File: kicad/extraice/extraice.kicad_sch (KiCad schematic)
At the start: 71 parts, among them J1 Conn_01x02, J10 Conn_01x02, J3 EncSide, J4 MainSide, J5 Conn_01x05, J6 EncSide, J7 MainSide, J8 Conn_01x02, J9 Conn_01x02, Q1 L-31ROPT1C, Q2 L-31ROPT1C, Q3 L-31ROPT1C, Q4 L-31ROPT1C, SW1 PCM12SMTR, SW2 B3U-1000P, U1 DG2034EDN, U10 DRV8837C, U11 DRV8837C, U12 AS5047D, U2 BCR421, U3 MUN12AD01-SG, U4 MB85RC64TA, U5 LSM6DSR, U6 XC6221B302GR, U7 ESP32-S3-FN8, U8 AS5047D, U9 DRV8837C, X1 830108208709

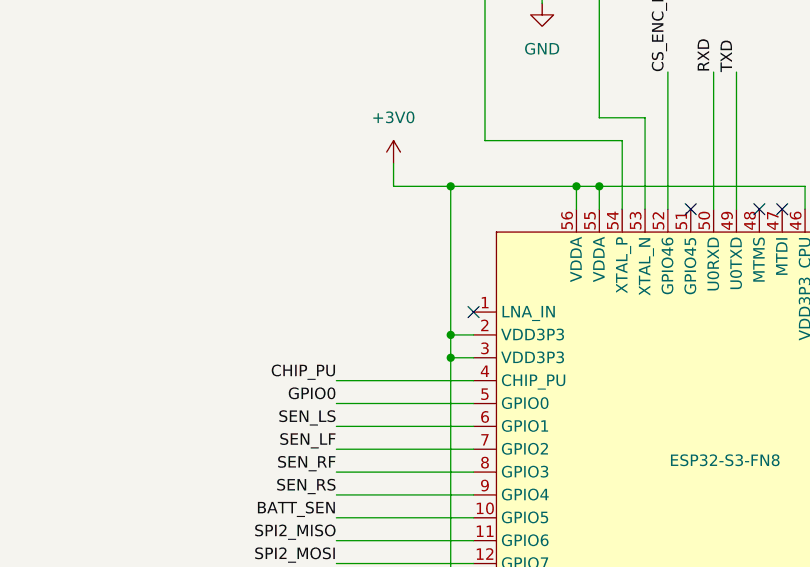
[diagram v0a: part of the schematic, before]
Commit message: Add a pull-up register to the CHIP-PU pin.
Signed-off-by: Kazuki Iida <elkel53930@gmail.com>
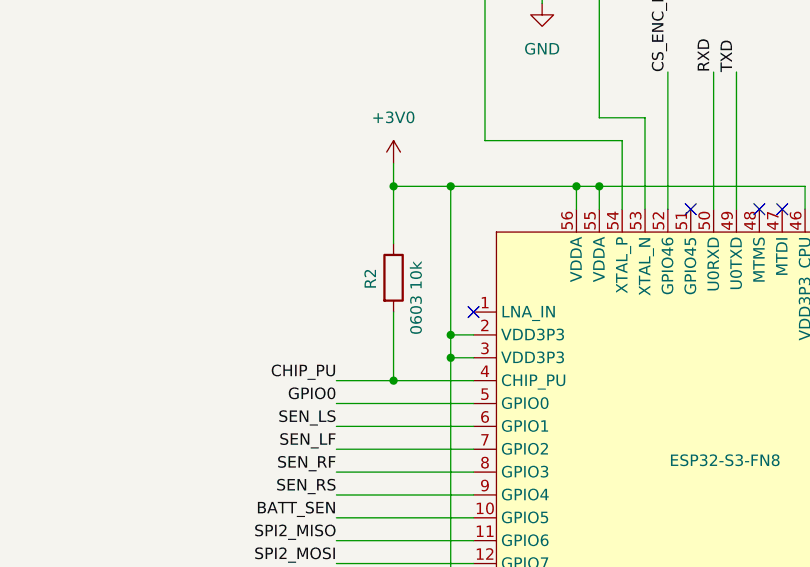
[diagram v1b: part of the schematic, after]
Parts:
- added R2: 0603 10k, Resistor_SMD:R_0201_0603Metric, symbol Device:R
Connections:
- net +3V0: now also R2.1
- net CHIP_PU: now also R2.2
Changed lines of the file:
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@@
   (junction (at 158.75 168.91) (diameter 0) (color 0 0 0 0)
   )
+  (junction (at 209.55 125.73) (diameter 0) (color 0 0 0 0)
+  )
   (junction (at 281.94 234.95) (diameter 0) (color 0 0 0 0)
   )
@@
   (junction (at 91.44 237.49) (diameter 0) (color 0 0 0 0)
   )
+  (junction (at 209.55 104.14) (diameter 0) (color 0 0 0 0)
+  )
   (junction (at 189.23 180.34) (diameter 0) (color 0 0 0 0)
   )
@@
     (stroke (width 0) (type default))
   )
+  (wire (pts (xy 209.55 118.11) (xy 209.55 125.73))
+    (stroke (width 0) (type default))
+  )
   (wire (pts (xy 68.58 232.41) (xy 71.12 232.41))
     (stroke (width 0) (type default))
@@
     (stroke (width 0) (type default))
   )
-  (wire (pts (xy 203.2 125.73) (xy 218.44 125.73))
+  (wire (pts (xy 203.2 125.73) (xy 209.55 125.73))
     (stroke (width 0) (type default))
   )
@@
     (stroke (width 0) (type default))
   )
+  (wire (pts (xy 209.55 125.73) (xy 218.44 125.73))
+    (stroke (width 0) (type default))
+  )
   (wire (pts (xy 377.19 107.95) (xy 375.92 107.95))
     (stroke (width 0) (type default))
@@
     (stroke (width 0) (type default))
   )
+  (wire (pts (xy 209.55 104.14) (xy 209.55 110.49))
+    (stroke (width 0) (type default))
+  )
   (wire (pts (xy 375.92 158.75) (xy 375.92 165.1))
     (stroke (width 0) (type default))
@@
         )
       )
+    )
+  )
+  (symbol (lib_id "Device:R") (at 209.55 114.3 0) (unit 1)
+    (in_bom yes) (on_board yes) (dnp no)
+    (property "Reference" "R2" (at 207.01 115.57 90)
+      (effects (font (size 1.27 1.27)) (justify left))
+    )
+    (property "Value" "0603 10k" (at 212.09 120.65 90)
+      (effects (font (size 1.27 1.27)) (justify left))
+    )
+    (property "Footprint" "Resistor_SMD:R_0201_0603Metric" (at 207.772 114.3 90)
+      (effects (font (size 1.27 1.27)) hide)
+    )
+    (property "Datasheet" "~" (at 209.55 114.3 0)
+      (effects (font (size 1.27 1.27)) hide)
+    )
+    (pin "1")
+    (pin "2")
+    (instances
+      (project "extraice"
+        (path "/758e42d9-0381-4d70-87c4-16282301b5b4"
+          (reference "R2") (unit 1)
+        )
+      )

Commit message: Artwork for 4A completed
Need to check details.

Signed-off-by: Kazuki Iida <elkel53930@gmail.com>
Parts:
- removed C14, C15, C16, C5: 0603 50V 0.1uF, Capacitor_SMD:C_0201_0603Metric, symbol Device:C_Small
- removed J1: Conn_01x02, Micromouse:B2B-ZH, symbol Connector_Generic:Conn_01x02
- removed R14, R15, R16: 0603 10k, Resistor_SMD:R_0201_0603Metric, symbol Device:R
- removed SW2: B3U-1000P, Button_Switch_SMD:SW_SPST_B3U-1000P, symbol Switch:SW_Push
- removed U4: MB85RC64TA, Library:LCC-8P-M04, symbol micromouse:MB85RC64TA
- removed X1: 830108208709, Oscillator:Oscillator_SMD_ECS_2520MV-xxx-xx-4Pin_2.5x2.0mm, symbol Device:Crystal_GND24
- added C6: 1608 10V 4.7uF, Capacitor_SMD:C_0603_1608Metric, symbol Device:C_Small
- added D8: 1608 R LED, LED_SMD:LED_0603_1608Metric, symbol Device:LED
- added J1, J2: Conn_01x03, Connector_PinHeader_2.00mm:PinHeader_1x03_P2.00mm_Vertical, symbol Connector_Generic:Conn_01x03
- added R3: 0603 10k, Resistor_SMD:R_0201_0603Metric, symbol Device:R
- C11, C13: value 1005 N/M -> 1608 10V 4.7uF; footprint Capacitor_SMD:C_0402_1005Metric -> Capacitor_SMD:C_0603_1608Metric
- C12: value 0603 50V 0.1uF -> 1608 10V 4.7uF; footprint Capacitor_SMD:C_0201_0603Metric -> Capacitor_SMD:C_0603_1608Metric
- C4: value 3225 25V 22uF -> 1608 10V 4.7uF; footprint Capacitor_SMD:C_1210_3225Metric -> Capacitor_SMD:C_0603_1608Metric
- R1, R10, R12, R7: value 0603 470 1% -> 1005 470 1%; footprint Resistor_SMD:R_0201_0603Metric -> Resistor_SMD:R_0402_1005Metric
- U7: value ESP32-S3-FN8 -> ESP32-S3-PICO-1-N8R2
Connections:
- net +3.3V: now also C11.2, C12.2, C13.2, C4.2, C6.2; no longer C4.1
- net +3V0: no longer C12.1
- net +BATT: now also SW1.2 (B), R3.2; no longer C21.1, SW1.3 (C), U10.1 (VM), U11.1 (VM), U9.1 (VM)
- net CS_ENC_L: now also U7.14 (GPIO9); no longer U7.15 (GPIO10)
- net CS_IMU: now also U7.27 (GPIO21); no longer U7.14 (GPIO9)
- net GND: now also C11.1, C12.1, C13.1, C4.1, C6.1, D8.1 (K), J2.1 (Pin_1); no longer C11.2, C12.2, C13.2, C4.2
- net LED_SEL0: now also U7.12 (GPIO7); no longer U7.21 (XTAL_32K_P)
- net LED_SEL1: now also U7.13 (GPIO8); no longer U7.22 (XTAL_32K_N)
- net SEN_LED_ENA: now also U7.11 (GPIO6); no longer U7.19 (GPIO14)
- net SEN_LF: now also U7.8 (GPIO3); no longer U7.7 (GPIO2)
- net SEN_LS: now also U7.9 (GPIO4); no longer U7.6 (GPIO1)
- net SEN_RF: now also U7.7 (GPIO2); no longer U7.8 (GPIO3)
- net SEN_RS: now also U7.6 (GPIO1); no longer U7.9 (GPIO4)
- net SPI1_MISO: now also U7.16 (GPIO11); no longer U7.17 (GPIO12)
- net SPI1_MOSI: now also U7.17 (GPIO12); no longer U7.18 (GPIO13)
- net SPI1_SCK: now also U7.15 (GPIO10); no longer U7.16 (GPIO11)
- net SPI2_MISO: now also U7.22 (XTAL_32K_N); no longer U7.11 (GPIO6)
- net SPI2_MOSI: now also U7.25 (GPIO19); no longer U7.12 (GPIO7)
- net SPI2_SCK: now also U7.26 (GPIO20); no longer U7.13 (GPIO8)
- net at U7.54 (XTAL_P): no longer C11.1
- net at U7.53 (XTAL_N): no longer C13.1
- net LED_FRONT_B renamed LED_B
- net LED_B: now also U7.21 (XTAL_32K_P); no longer U7.26 (GPIO20)
- net LED_LEFT_R renamed LED_R
- net LED_R: now also U7.18 (GPIO13); no longer U7.27 (GPIO21)
- net LED_RIGHT_G renamed LED_G
- net LED_G: now also U7.19 (GPIO14); no longer U7.25 (GPIO19)
- net SCL: no longer names the net of U7.23 (GPIO17)
- net SDA: no longer names the net of U7.24 (GPIO18)
- new net: D8.2 (A), R3.1
- new net: J1.1 (Pin_1), J2.3 (Pin_3)
- new net V_MOT: C21.1, J1.3 (Pin_3), SW1.3 (C), U10.1 (VM), U11.1 (VM), U9.1 (VM)
- no-connect marks 34 -> 40
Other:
- note removed: "Log storage"
- moved on the sheet: C10, C18, C19, D5, D6, D7, R2, R4, R5, R6, SW1, U6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

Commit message: EXTRAICE5
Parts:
- removed C19, C3: 0603 50V 0.1uF, Capacitor_SMD:C_0201_0603Metric, symbol Device:C_Small
- removed C2, C21: 2012 35V 10uF, Capacitor_SMD:C_0805_2012Metric, symbol Device:C_Small
- removed C6: 1608 10V 4.7uF, Capacitor_SMD:C_0603_1608Metric, symbol Device:C_Small
- removed D1, D3, D4: OSI5FU3A11C, Micromouse:OSI5FU3A11C, symbol Device:LED
- removed J10, J8, J9: Conn_01x02, Micromouse:MotorPad, symbol Connector_Generic:Conn_01x02
- removed Q1, Q2, Q3, Q4: L-31ROPT1C, Micromouse:OSI5FU3A11C, symbol Device:Q_Photo_NPN_CE
- removed R11: 0603 6.2, Resistor_SMD:R_0201_0603Metric, symbol Device:R
- removed R13: 0603 22k, Resistor_SMD:R_0201_0603Metric, symbol Device:R
- removed R2: 0603 10k, Resistor_SMD:R_0201_0603Metric, symbol Device:R
- removed U10, U11, U9: DRV8837C, Package_SON:WSON-8-1EP_2x2mm_P0.5mm_EP0.9x1.6mm, symbol Driver_Motor:DRV8837C
- removed U3: MUN12AD01-SG, Library:MUN12AD01-SG, symbol micromouse:MUN12AD01-SG
- added BT1: 100mAh LiPo, Micromouse:Battery, symbol Device:Battery_Cell
- added C11, C14, C15, C16: 1005 50V 0.1uF, Capacitor_SMD:C_0402_1005Metric, symbol Device:C_Small
- added C17: 2012 35V 10uF, Capacitor_SMD:C_0805_2012Metric, symbol Device:C_Small
- added C5, C8: 4532 10u 16V, Capacitor_SMD:C_1812_4532Metric, symbol Device:C_Small
- added D3: BAS516, Diode_SMD:D_SOD-523, symbol Diode:BAS516
- added D5, D8: 1608 LED, LED_SMD:LED_0603_1608Metric, symbol Device:LED
- added H5, H6: Φ2.2, MountingHole:MountingHole_2.2mm_M2, symbol Mechanical:MountingHole
- added J10, J11: Conn_01x03, Connector_PinSocket_2.00mm:PinSocket_1x03_P2.00mm_Vertical, symbol Connector_Generic:Conn_01x03
- added J12: Conn_01x02, Micromouse:B2B-ZH, symbol Connector_Generic:Conn_01x02
- added J4, J5: Conn_01x02, Connector_PinHeader_1.27mm:PinHeader_1x02_P1.27mm_Vertical, symbol Connector_Generic:Conn_01x02
- added LS1: SMT-0440-T-2-R, Library:SMT-0440-T-2-R, symbol Device:Speaker
- added Q1: MMBT3904, Package_TO_SOT_SMD:SOT-23, symbol Transistor_BJT:MMBT3904
- added R14, R20, R3: 1005 10k, Resistor_SMD:R_0402_1005Metric, symbol Device:R
- added R15, R16, R17, R18, R21, R4: 1005 1k, Resistor_SMD:R_0402_1005Metric, symbol Device:R
- added R19: 1005 6.2, Resistor_SMD:R_0402_1005Metric, symbol Device:R
- added R7: 1005 470 1%, Resistor_SMD:R_0402_1005Metric, symbol Device:R
- added U12, U13: ~, Micromouse:PhotoSensorL, symbol micromouse:PhotorSensor
- added U14, U15: ~, Micromouse:PhotoSensorR, symbol micromouse:PhotorSensor
- added U16: LTC4054ES5-4.2, Package_TO_SOT_SMD:TSOT-23-5, symbol Battery_Management:LTC4054ES5-4.2
- added U2, U5: DRV8837C, Package_SON:WSON-8-1EP_2x2mm_P0.5mm_EP0.9x1.6mm, symbol Driver_Motor:DRV8837C
- added U4: TLA2528IRTER, Package_DFN_QFN:WQFN-16-1EP_3x3mm_P0.5mm_EP1.68x1.68mm, symbol micromouse:TLA2528
- added U5: MB85RC64TA, Library:LCC-8P-M04, symbol micromouse:MB85RC64TA
- C10: value 1608 35V 1uF -> 1005 50V 0.1uF; footprint Capacitor_SMD:C_0603_1608Metric -> Capacitor_SMD:C_0402_1005Metric
- C13: renamed from C8; value 0603 50V 0.1uF -> 1005 50V 0.1uF; footprint Capacitor_SMD:C_0201_0603Metric -> Capacitor_SMD:C_0402_1005Metric
- C4: value 1608 10V 4.7uF -> 4532 10u 16V; footprint Capacitor_SMD:C_0603_1608Metric -> Capacitor_SMD:C_1812_4532Metric; フィールド4 (none) -> 16MU106MC44532
- C7: value 0603 50V 0.1uF -> 1005 50V 0.1uF; footprint Capacitor_SMD:C_0201_0603Metric -> Capacitor_SMD:C_0402_1005Metric
- C9: value 0603 50V 0.1uF -> 1608 35V 1uF; footprint Capacitor_SMD:C_0201_0603Metric -> Capacitor_SMD:C_0603_1608Metric
- D1: renamed from D5; value 1608 R LED -> 1608 LED
- D2: value OSI5FU3A11C -> 1608 LED; footprint Micromouse:OSI5FU3A11C -> LED_SMD:LED_0603_1608Metric
- D6: value 1608 G LED -> 1608 LED
- D7: value 1608 B LED -> 1608 LED
- R1: renamed from R4; value 0603 1k -> 1005 1k; footprint Resistor_SMD:R_0201_0603Metric -> Resistor_SMD:R_0402_1005Metric
- R2: renamed from R3; value 0603 10k -> 1005 10k; footprint Resistor_SMD:R_0201_0603Metric -> Resistor_SMD:R_0402_1005Metric
- R5: value 0603 1k -> 1005 10k; footprint Resistor_SMD:R_0201_0603Metric -> Resistor_SMD:R_0402_1005Metric
- R6, R9: value 0603 1k -> 1005 1k; footprint Resistor_SMD:R_0201_0603Metric -> Resistor_SMD:R_0402_1005Metric
- R8: value 0603 10k -> 1005 1k; footprint Resistor_SMD:R_0201_0603Metric -> Resistor_SMD:R_0402_1005Metric
- renumbered C11 to C1, C1 to C12, C12 to C2, C13 to C3, C18 to C6, D8 to D4, H3 to H2, H2 to H3, J5 to J3, J3 to J6, J4 to J7, J6 to J8, J7 to J9, R1 to R10, R7 to R11, R10 to R12, R12 to R13, U6 to U1, U1 to U10, U2 to U11, U7 to U3, U8 to U7, U12 to U8, U5 to U9
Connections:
- net PWM_V is gone; now on net MOT_SLEEP: U3.38 (GPIO33)
- net +3V0: now also C4.1, C7.1, D1.2 (A), D2.2 (A), D6.2 (A), D7.2 (A), C11.1, C15.1, C16.1, D3.1 (K), D5.2 (A), LS1.1, R14.2, R15.2, R16.2, R17.2, R18.2, U12.2, U13.2, U14.2, U15.2, U4.10 (DVDD), U4.7 (AVDD), U5.8 (VDD); no longer C10.1, C13.2, C7.2, C9.1, R1.1, R5.1, R6.1
- net +BATT: now also C1.2, C12.1, C2.2, C3.2, U1.1 (VIN), U1.3 (CE), U10.4 (EN), U10.6 (V+), R3.2, U12.3, U13.3, U14.3, U15.3; no longer R8.2
- net BATT_SEN: now also R5.2, R3.1, U4.15 (AIN0/GPIO0); no longer R8.1, R9.2, U3.10 (GPIO5)
- net CHIP_PU: now also R14.1
- net CS_ENC_L: now also U3.17 (GPIO12); no longer U3.14 (GPIO9)
- net CS_IMU: now also U3.13 (GPIO8); no longer U3.27 (GPIO21)
- net CWCCW_L: now also U5.5 (IN2)
- net CWCCW_R: now also U2.5 (IN2)
- net GND: now also C4.2, C7.2, C9.1, J2.2 (Pin_2), J2.3 (Pin_3), R5.1, C11.2, C15.2, C16.2, C5.2, C8.2, Q1.2 (E), R19.1, U2.4 (GND), U2.9 (GND), U4.17 (THPD), U4.9 (GND), U5.1 (A0), U5.2 (A1), U5.3 (A2), U5.4 (GND), U5.4 (VSS), U5.9 (GND); no longer C13.1, C4.1, C7.1, C9.2, R9.1
- net LED_SEL0: now also U4.4 (AIN5/GPIO5); no longer U3.12 (GPIO7)
- net LED_SEL1: now also U4.5 (AIN6/GPIO6); no longer U3.13 (GPIO8)
- net MOT_SLEEP: now also U2.7 (~{SLEEP}), U5.7 (~{SLEEP}); no longer U3.43 (GPIO38)
- net PWM_L: now also U5.6 (IN1)
- net PWM_R: now also U2.6 (IN1)
- net SEN_LED_ENA: now also U4.6 (AIN7/GPIO7); no longer U3.11 (GPIO6)
- net SEN_LF: now also R10.1, U12.1, U4.3 (AIN4/GPIO4); no longer R11.1, U3.8 (GPIO3)
- net SEN_LS: now also R11.1, U13.1, U4.2 (AIN3/GPIO3); no longer R10.1, U3.9 (GPIO4)
- net SEN_RF: now also R13.1, U15.1, U4.16 (AIN1/GPIO1); no longer R12.1, U3.7 (GPIO2)
- net SEN_RS: now also R12.1, U14.1, U4.1 (AIN2/GPIO2); no longer R13.1, U3.6 (GPIO1)
- net SPI1_MISO: now also U3.15 (GPIO10); no longer U3.16 (GPIO11)
- net SPI1_MOSI: now also U3.14 (GPIO9); no longer U3.17 (GPIO12)
- net SPI1_SCK: now also U3.16 (GPIO11); no longer U3.15 (GPIO10)
- net SPI2_MISO: now also U3.10 (GPIO5); no longer U3.22 (XTAL_32K_N)
- net SPI2_MOSI: now also U3.11 (GPIO6); no longer U3.25 (GPIO19)
- net SPI2_SCK: now also U3.12 (GPIO7); no longer U3.26 (GPIO20)
- net V_MOT: now also J1.1 (Pin_1), J1.2 (Pin_2), C5.1, C8.1, U2.1 (VM), U2.8 (VCC), U5.1 (VM), U5.8 (VCC)
- net LED_2: now reaches R6.2
- net LED_2: now also U3.25 (GPIO19); no longer D7.2 (A)
- net at J8.1 (Pin_1), U8.12 (VDD3V3): now also C14.1
- net at J8.6 (Pin_6), U8.13 (GND), U8.5 (TST): now also C14.2
- net at D2.1 (K): now also R4.1; no longer U10.7 (S4)
- net at U11.6 (Rext): now also R19.2
- net at J6.1 (Pin_1), U7.12 (VDD3V3): now also C13.1
- net at J6.6 (Pin_6), U7.13 (GND), U7.5 (TST): now also C13.2
- net at U10.3 (S3): now also U14.4
- net LED_0: now reaches R1.2
- net LED_0: now also U3.23 (GPIO17); no longer D1.2 (A)
- net at U10.9 (S2): now also U12.4
- net LED_1: now reaches U3.24 (GPIO18)
- net LED_1: now also R4.2
- net at U3.29 (VDD_SPI): now also C10.1
- net at U10.1 (S1): now also U15.4
- removed net +3.3V: C1.2, C12.1, C2.2, C3.2, C4.2, D2.2 (A), U1.1 (VIN), U1.3 (CE), U10.4 (EN), U10.6 (V+)
- net LED_B: no longer names the net of D7.1 (K)
- net LED_B: now also R9.1; no longer U3.21 (XTAL_32K_P)
- net LED_G: no longer names the net of D6.1 (K)
- net LED_G: now also R8.1; no longer U3.19 (GPIO14)
- net LED_R: no longer names the net of D1.1 (K)
- net LED_R: now also R1.1; no longer U3.18 (GPIO13)
- new net: C9.2, U4.8 (DECAP)
- new net: J4.1 (Pin_1), U2.2 (OUT1)
- new net: J4.2 (Pin_2), U2.3 (OUT2)
- new net: BT1.1 (+), J10.1 (Pin_1), J10.2 (Pin_2), J10.3 (Pin_3), U16.3 (BAT)
- new net: BT1.2 (-), C17.2, J11.1 (Pin_1), J11.2 (Pin_2), J11.3 (Pin_3), J12.1 (Pin_1), R20.1, U16.2 (GND)
- new net: R21.1, U16.1 (~{CHRG})
- new net: C17.1, D8.2 (A), J12.2 (Pin_2), U16.4 (V_{CC})
- new net: R20.2, U16.5 (PROG)
- new net: D3.2 (A), LS1.2, Q1.3 (C)
- new net: Q1.1 (B), R7.2
- new net: D8.1 (K), R21.2
- new net: D5.1 (K), R6.1
- new net: J5.1 (Pin_1), U5.2 (OUT1)
- new net: J5.2 (Pin_2), U5.3 (OUT2)
- new net: U10.7 (S4), U13.4
- new net BUZZ: R7.1, U3.43 (GPIO38)
- new net LED_3: R8.2, U3.26 (GPIO20)
- new net LED_4: R9.2, U3.27 (GPIO21)
- new net SCL0: R16.1, U3.9 (GPIO4), U4.13 (SCL)
- new net SCL1: R18.1, U3.19 (GPIO14), U5.5 (SDA)
- new net SDA0: R15.1, U3.8 (GPIO3), U4.14 (SDA)
- new net SDA1: R17.1, U3.18 (GPIO13), U5.6 (SCL)
- no-connect marks 40 -> 43
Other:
- note added: "Buzzer"
- note added: "I2C Adrs = 10h"
- note added: "I2C Adrs = 50h"
- note added: "Log storage"
- note added: "Wall sensor controller"
- note removed: "3.33V"
- note removed: "Fan motor"
- note removed: "L motor"
- note removed: "R motor"
- moved on the sheet: C1, C12, C13, C2, C3, C6, D1, D4, J1, J2, J3, R1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
